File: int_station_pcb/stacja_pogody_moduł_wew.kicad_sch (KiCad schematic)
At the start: 50 parts, among them J1 10118194-0001LF, J2 USB_C_Receptacle_USB2.0_16P, J3 Conn_01x06, Q1 NPN, Q2 NPN, SW1 SW_Push_Dual_x2, SW2 SW_Push_Dual_x2, SW3 SW_Push_Dual_x2, SW4 SW_Push_Dual_x2, U1 NRF24L01_Breakout, U3 LM39101RS-3.3V, U4 ESP32-WROOM-32E-N4, U5 CH340G, U6 USBLC6-2SC6, U7 USBLC6-2SC6, Y1 Crystal_GND24

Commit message: poprawa plytki wew i zew
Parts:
- removed C3: 10u, Capacitor_SMD:C_0805_2012Metric_Pad1.18x1.45mm_HandSolder, symbol Device:C
- added C12: 22u, Capacitor_Tantalum_SMD:CP_EIA-3528-21_Kemet-B_HandSolder, symbol Device:C_Polarized_Small
- added C4, C5: 10u, Capacitor_SMD:C_0805_2012Metric_Pad1.18x1.45mm_HandSolder, symbol Device:C
- renumbered C5 to C1, C2 to C10, C9 to C11, C12 to C13, C13 to C14, C4 to C2, C6 to C3, C1 to C6, C10 to C8, C11 to C9, D3 to D2, D2 to D3, J3 to J2, J2 to J3, R4 to R1, R9 to R10, R10 to R12, R14 to R13, R12 to R14, R18 to R15, R13 to R16, R3 to R2, R5 to R3, R6 to R4, R15 to R5, R16 to R6, R17 to R7, R7 to R8, R8 to R9, SW4 to SW3, SW3 to SW4, U6 to U1, U4 to U2, U2 to U3, U7 to U4, U1 to U5, U5 to U6, U3 to U7
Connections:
- net GND: now also C12.2, C4.1, C5.1
- net V_3.3_OUT: now also C12.1, C4.2, C5.2

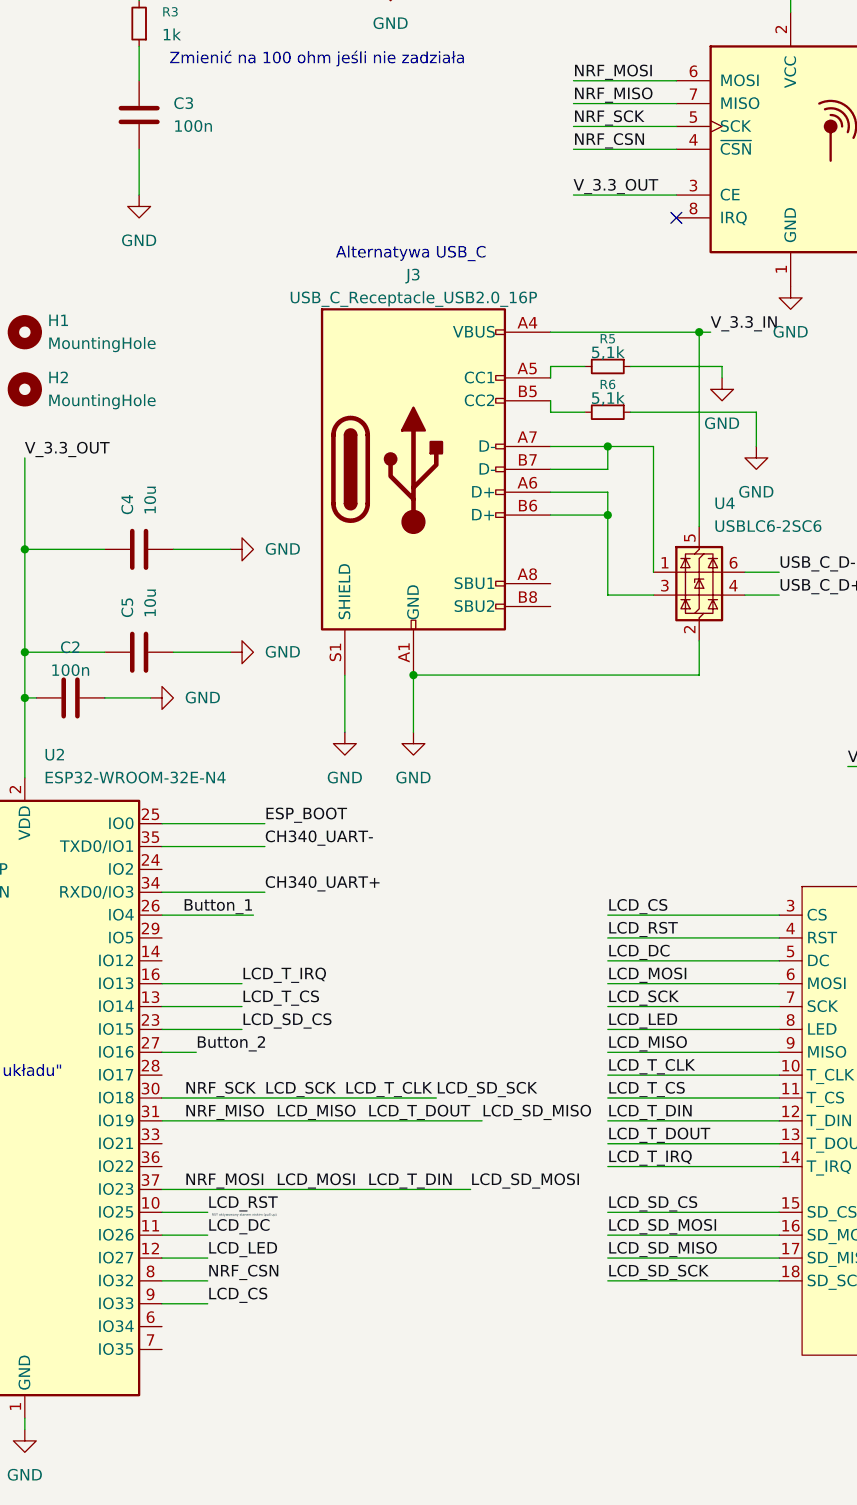
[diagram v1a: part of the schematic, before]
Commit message: powiekszyc sciezki do 0.2mm w wew
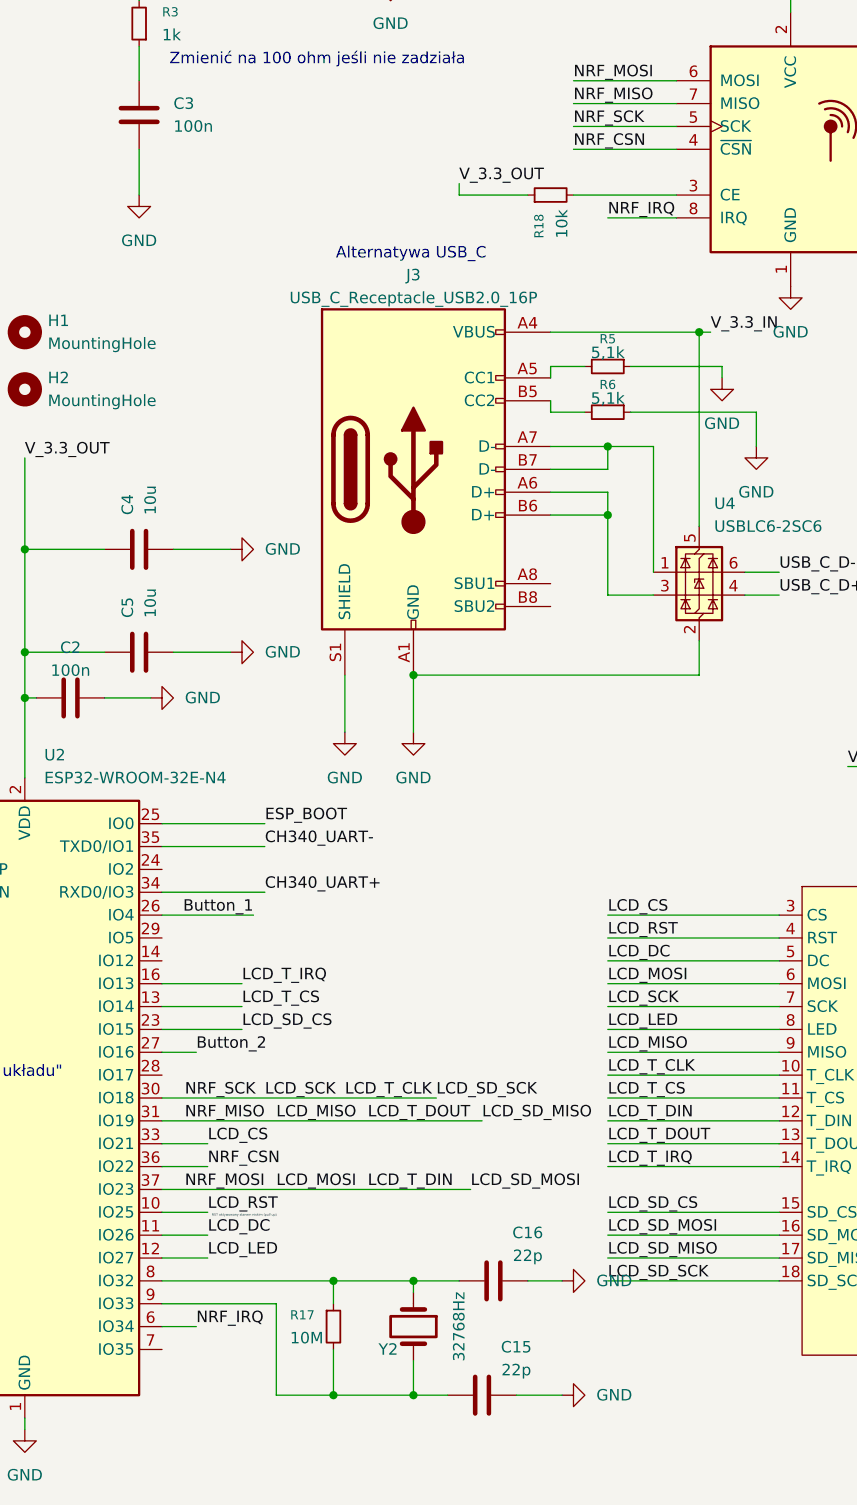
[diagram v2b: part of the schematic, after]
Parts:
- added C15, C16: 22p, Capacitor_SMD:C_0603_1608Metric_Pad1.08x0.95mm_HandSolder, symbol Device:C
- added R17: 10M, Resistor_SMD:R_0603_1608Metric, symbol Device:R_Small
- added R18: 10k, Resistor_SMD:R_0603_1608Metric, symbol Device:R_Small
- added Y2: 32768Hz, Crystal:Crystal_DS26_D2.0mm_L6.0mm_Horizontal, symbol Device:Crystal
- J3: footprint wyświetlacz lcd:USB_C_Receptacle_TME -> Connector_USB:USB_C_Receptacle_GCT_USB4105-xx-A_16P_TopMnt_Horizontal
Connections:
- net GND: now also C15.1, C16.1
- net LCD_CS: now also U2.33 (IO21); no longer U2.9 (IO33)
- net NRF_CSN: now also U2.36 (IO22); no longer U2.8 (IO32)
- net V_3.3_OUT: now also R18.1; no longer U5.3 (CE)
- net NRF_IRQ: now reaches U2.6 (IO34)
- net NRF_IRQ: now also U5.8 (IRQ)
- new net: C16.2, R17.1, U2.8 (IO32), Y2.1
- new net: C15.2, R17.2, U2.9 (IO33), Y2.2
- new net: R18.2, U5.3 (CE)
- no-connect marks 7 -> 6

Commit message: skonczona plytka wewnetrzna
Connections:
- net LCD_SD_CS: now also U2.24 (IO2); no longer U2.23 (IO15)
- net V_3.3_OUT: no longer R18.1
- net NRF_CE: now reaches U2.28 (IO17)
- net NRF_CE: now also R18.1
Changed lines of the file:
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@@
-	(wire
-		(pts
-			(xy 118.11 53.34) (xy 118.11 54.61)
-		)
-		(stroke
-			(width 0)
-			(type default)
-		)
-	)
 	(wire
 		(pts
@@
 	(wire
 		(pts
+			(xy 85.09 129.54) (xy 96.52 129.54)
+		)
+		(stroke
+			(width 0)
+			(type default)
+		)
+	)
+	(wire
+		(pts
 			(xy 205.74 38.1) (xy 205.74 44.45)
 		)
@@
 		(pts
 			(xy 163.83 30.48) (xy 168.91 30.48)
+		)
+		(stroke
+			(width 0)
+			(type default)
+		)
+	)
+	(wire
+		(pts
+			(xy 85.09 152.4) (xy 88.9 152.4)
 		)
 		(stroke
@@
 		)
 	)
+	(label "NRF_CE"
+		(at 118.11 54.61 0)
+		(effects
+			(font
+				(size 1.27 1.27)
+			)
+			(justify left bottom)
+		)
+	)
 	(label "NRF_MISO"
 		(at 87.63 157.48 0)
@@
 		)
 	)
-	(label "V_3.3_OUT"
-		(at 118.11 53.34 0)
-		(effects
-			(font
-				(size 1.27 1.27)
-			)
-			(justify left bottom)
-		)
-	)
 	(label "LCD_SD_MOSI"
 		(at 134.62 170.18 0)
@@
 	)
 	(label "LCD_SD_CS"
-		(at 93.98 147.32 0)
+		(at 96.52 129.54 0)
 		(effects
 			(font
@@
 		)
 	)
+	(label "NRF_CE"
+		(at 88.9 152.4 0)
+		(effects
+			(font
+				(size 1.27 1.27)
+			)
+			(justify left bottom)
+		)
+	)

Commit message: poprawa footprintu usb
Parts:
- J3: footprint Connector_USB:USB_C_Receptacle_GCT_USB4105-xx-A_16P_TopMnt_Horizontal -> wyświetlacz lcd:USB_C_Receptacle_TME
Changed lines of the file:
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@@
 			)
 		)
-		(property "Footprint" "Connector_USB:USB_C_Receptacle_GCT_USB4105-xx-A_16P_TopMnt_Horizontal"
+		(property "Footprint" "wyświetlacz lcd:USB_C_Receptacle_TME"
 			(at 116.84 85.09 0)
 			(effects

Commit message: photos of project
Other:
- note added: "Additional connector for external programmer"
- note added: "Alternative microUSB supply"
- note added: "Communication with external sensor"
- note added: "ERROR FLAGE diode (3.3 V power supply)"
- note added: "ESP boot diode"
- note added: "ESP enable diode"
- note added: "LCD display"
- note added: "MCU"
- note added: "Power supply 3.3 V"
- note added: "USB -> ESP32 communication"
- note added: "USB-C 5V power supply"
- note removed: ""Serce układu""
- note removed: "Alternatywa USB_C"
- note removed: "Automatyczny reset z możliwością przycisku"
- note removed: "Dioda do ERROR FLAGE przetwornika 3,3 V"
- note removed: "Dioda do boot ESP"
- note removed: "Dioda do enable ESP"
- note removed: "Komunikacja USB z ESP32"
- note removed: "Komunikacja z modułem zewnętrznym"
- note removed: "Przetwornica 3.3 V"
- note removed: "Przycisk do zmiany jasności ekranu (PWM)"
- note removed: "RST aktywowany stanem niskim (pull up)"
- note removed: "Wybór trybu pracy"
- note removed: "Wyświetlacz LCD do pomiarów + wykres"
- note removed: "Zasialnie microusb"
- note removed: "Zmiana trybu pracy wyświetlacza (wykres lub pomiary)"
- note removed: "Zmienić na 100 ohm jeśli nie zadziała"
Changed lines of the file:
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@@
 	(generator_version "9.0")
 	(paper "A4")
-	(text "Wyświetlacz LCD do pomiarów + wykres"
+	(text "LCD display"
 		(exclude_from_sim no)
 		(at 169.672 157.226 90)
@@
 		)
 	)
-	(text "Komunikacja z modułem zewnętrznym"
+	(text "Communication with external sensor"
 		(exclude_from_sim no)
 		(at 156.21 15.494 0)
@@
 		)
 	)
-	(text "Zmienić na 100 ohm jeśli nie zadziała"
+	(text "Alternative microUSB supply"
 		(exclude_from_sim no)
-		(at 102.362 39.624 0)
+		(at 23.876 68.326 0)
 		(effects
 			(font
@@
 		)
 	)
-	(text "Zasialnie microusb"
+	(text "ESP enable diode"
 		(exclude_from_sim no)
-		(at 23.114 68.072 0)
+		(at 276.606 140.462 0)
 		(effects
 			(font
@@
 		)
 	)
-	(text "Wybór trybu pracy "
+	(text "Additional connector for external programmer"
 		(exclude_from_sim no)
-		(at 270.256 92.71 0)
+		(at 26.924 143.256 0)
 		(effects
 			(font
@@
 		)
 	)
-	(text "Dioda do enable ESP"
+	(text "ESP boot diode"
 		(exclude_from_sim no)
-		(at 278.13 138.938 0)
+		(at 256.286 140.208 0)
 		(effects
 			(font
@@
 		)
 	)
-	(text "Automatyczny reset z możliwością przycisku"
-		(exclude_from_sim no)
-		(at 258.826 13.97 0)
-		(effects
-			(font
-				(size 1.27 1.27)
-			)
-		)
-	)
-	(text "Dioda do boot ESP"
-		(exclude_from_sim no)
-		(at 256.286 138.938 0)
-		(effects
-			(font
-				(size 1.27 1.27)
-			)
-		)
-	)
-	(text "RST aktywowany stanem niskim (pull up)"
-		(exclude_from_sim no)
-		(at 94.234 168.148 0)
-		(effects
-			(font
-				(size 0.254 0.254)
-			)
-		)
-	)
-	(text "Alternatywa USB_C"
+	(text "USB-C 5V power supply\n"
 		(exclude_from_sim no)
 		(at 112.776 61.214 0)
@@
 		)
 	)
-	(text "Dioda do ERROR FLAGE przetwornika 3,3 V"
+	(text "ERROR FLAGE diode (3.3 V power supply)"
 		(exclude_from_sim no)
 		(at 282.702 109.982 0)
@@
 		)
 	)
-	(text "Komunikacja USB z ESP32\n"
+	(text "USB -> ESP32 communication\n"
 		(exclude_from_sim no)
-		(at 208.788 29.718 0)
+		(at 210.82 29.972 0)
 		(effects
 			(font
@@
 		)
 	)
-	(text "Zmiana trybu pracy wyświetlacza (wykres lub pomiary)"
-		(exclude_from_sim no)
-		(at 96.52 14.224 0)
-		(effects
-			(font
-				(size 1.27 1.27)
-			)
-		)
-	)
-	(text "Przycisk do zmiany jasności ekranu (PWM)"
-		(exclude_from_sim no)
-		(at 38.1 14.478 0)
-		(effects
-			(font
-				(size 1.27 1.27)
-			)
-		)
-	)
-	(text "\"Serce układu\""
+	(text "MCU\n"
 		(exclude_from_sim no)
 		(at 67.564 152.146 0)
@@
 		)
 	)
-	(text "Przetwornica 3.3 V"
+	(text "Power supply 3.3 V"
 		(exclude_from_sim no)
-		(at 214.884 134.366 0)
+		(at 214.63 132.842 0)
 		(effects
 			(font
-				(size 1.27 1.27)
-			)
-		)
-	)
-	(text "Zmienić na 100 ohm jeśli nie zadziała"
-		(exclude_from_sim no)
-		(at 45.212 39.624 0)
-		(effects
-			(font
